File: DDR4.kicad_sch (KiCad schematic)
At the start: 37 parts, among them U14 2199155-1

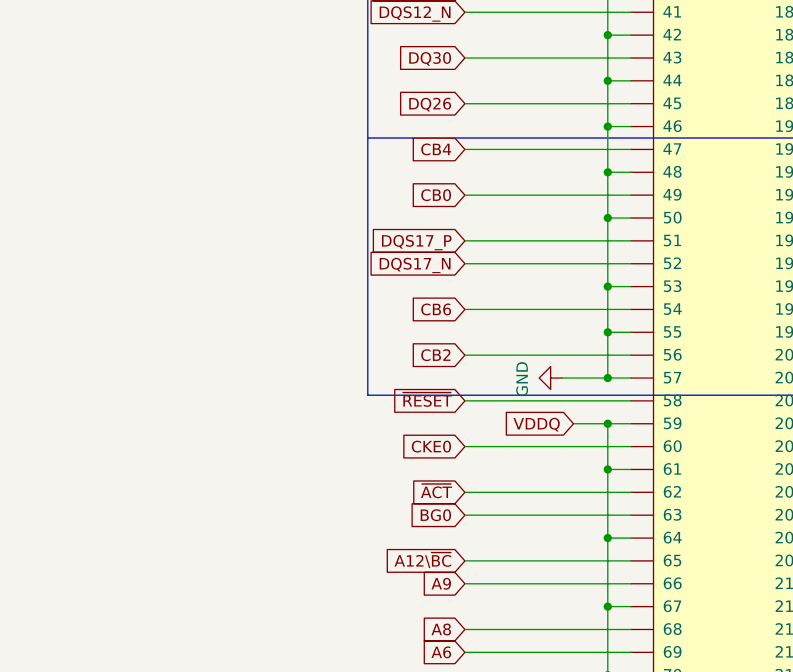
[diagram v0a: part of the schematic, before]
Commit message: Added hot-swap: button, LED indication, detection on ground pin. Updated SN74LVC1G07 symbol
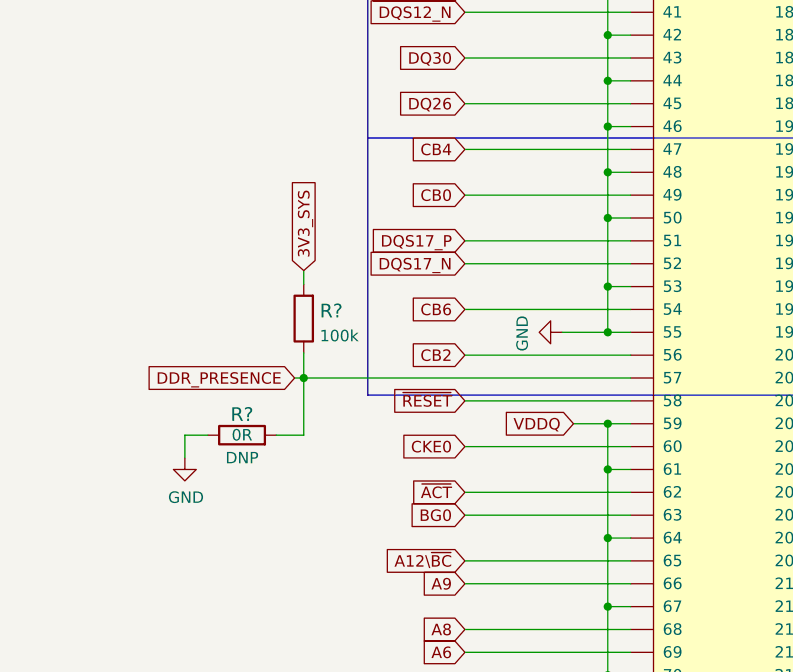
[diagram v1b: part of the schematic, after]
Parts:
- added R?: R_0R_0402, antmicro-footprints:0402-res, symbol antmicroResistors0402:R_0R_0402
- added R?: R_100k_0402, antmicro-footprints:0402-res, symbol antmicroResistors0402:R_100k_0402
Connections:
- net GND: now also R?.1; no longer U14.57
- new net 3V3_SYS: R?.2
- new net DDR_PRESENCE: R?.1, R?.2, U14.57
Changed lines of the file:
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@@
   (junction (at 125.73 168.91) (diameter 0) (color 0 0 0 0)
   )
-  (junction (at 97.79 194.31) (diameter 0) (color 0 0 0 0)
-  )
   (junction (at 97.79 189.23) (diameter 0) (color 0 0 0 0)
   )
@@
   (junction (at 125.73 179.07) (diameter 0) (color 0 0 0 0)
   )
+  (junction (at 64.008 194.31) (diameter 0) (color 0 0 0 0)
+  )
   (junction (at 259.715 175.895) (diameter 0) (color 0 0 0 0)
   )
@@
     (stroke (width 0) (type default) (color 0 0 0 0))
   )
-  (wire (pts (xy 97.79 194.31) (xy 92.71 194.31))
+  (wire (pts (xy 97.79 189.23) (xy 92.71 189.23))
     (stroke (width 0) (type default) (color 0 0 0 0))
   )
@@
     (stroke (width 0) (type default) (color 0 0 0 0))
   )
-  (wire (pts (xy 97.79 194.31) (xy 97.79 189.23))
-    (stroke (width 0) (type default) (color 0 0 0 0))
-  )
   (wire (pts (xy 259.715 86.995) (xy 259.715 81.915))
     (stroke (width 0) (type default) (color 0 0 0 0))
@@
     (stroke (width 0) (type default) (color 0 0 0 0))
   )
+  (wire (pts (xy 60.96 200.66) (xy 64.008 200.66))
+    (stroke (width 0) (type default) (color 0 0 0 0))
+  )
   (wire (pts (xy 287.655 137.795) (xy 285.115 137.795))
     (stroke (width 0) (type default) (color 0 0 0 0))
@@
     (stroke (width 0) (type default) (color 0 0 0 0))
   )
+  (wire (pts (xy 50.8 200.66) (xy 53.34 200.66))
+    (stroke (width 0) (type default) (color 0 0 0 0))
+  )
   (wire (pts (xy 285.115 219.075) (xy 303.53 219.075))
     (stroke (width 0) (type default) (color 0 0 0 0))
@@
     (stroke (width 0) (type default) (color 0 0 0 0))
   )
+  (wire (pts (xy 64.008 200.66) (xy 64.008 194.31))
+    (stroke (width 0) (type default) (color 0 0 0 0))
+  )
   (wire (pts (xy 123.19 242.57) (xy 128.27 242.57))
     (stroke (width 0) (type default) (color 0 0 0 0))
@@
     (stroke (width 0) (type default) (color 0 0 0 0))
   )
+  (wire (pts (xy 64.008 182.372) (xy 64.008 183.896))
+    (stroke (width 0) (type default) (color 0 0 0 0))
+  )
   (wire (pts (xy 287.655 155.575) (xy 287.655 160.655))
     (stroke (width 0) (type default) (color 0 0 0 0))
@@
     (stroke (width 0) (type default) (color 0 0 0 0))
   )
+  (wire (pts (xy 50.8 203.2) (xy 50.8 200.66))
+    (stroke (width 0) (type default) (color 0 0 0 0))
+  )
   (wire (pts (xy 97.79 128.27) (xy 97.79 120.65))
     (stroke (width 0) (type default) (color 0 0 0 0))
@@
     (stroke (width 0) (type default) (color 0 0 0 0))
   )
-  (wire (pts (xy 100.33 194.31) (xy 97.79 194.31))
+  (wire (pts (xy 64.008 194.31) (xy 100.33 194.31))
+    (stroke (width 0) (type default) (color 0 0 0 0))
+  )
+  (wire (pts (xy 62.992 194.31) (xy 64.008 194.31))
     (stroke (width 0) (type default) (color 0 0 0 0))
   )
@@
     (stroke (width 0) (type default) (color 0 0 0 0))
   )
+  (wire (pts (xy 64.008 194.31) (xy 64.008 191.516))
+    (stroke (width 0) (type default) (color 0 0 0 0))
+  )
   (wire (pts (xy 347.98 238.125) (xy 354.965 238.125))
     (stroke (width 0) (type default) (color 0 0 0 0))
@@
     )
   )
+  (global_label "3V3_SYS" (shape input) (at 64.008 182.372 90) (fields_autoplaced)
+    (effects (font (size 1.27 1.27)) (justify left))
+    (property "Intersheet References" "${INTERSHEET_REFS}" (id 0) (at -88.392 -29.083 0)
+      (effects (font (size 1.27 1.27)) hide)
+    )
+  )
   (global_label "DQ39" (shape input) (at 303.53 120.015 0) (fields_autoplaced)
     (effects (font (size 1.27 1.27)) (justify left))
@@
     )
   )
+  (global_label "DDR_PRESENCE" (shape input) (at 62.992 194.31 180) (fields_autoplaced)
+    (effects (font (size 1.27 1.27)) (justify right))
+    (property "Intersheet References" "${INTERSHEET_REFS}" (id 0) (at 46.093 194.2306 0)
+      (effects (font (size 1.27 1.27)) (justify right) hide)
+    )
+  )
   (global_label "~{SAVE}" (shape input) (at 303.53 76.835 0) (fields_autoplaced)
     (effects (font (size 1.27 1.27)) (justify left))
@@
     (pin "1")
   )
-  (symbol (lib_id "data-center-dram-tester:GND") (at 92.71 194.31 270) (unit 1)
+  (symbol (lib_id "data-center-dram-tester:GND") (at 92.71 189.23 270) (unit 1)
     (in_bom yes) (on_board yes)
-    (property "Reference" "#PWR0150" (id 0) (at 86.36 194.31 0)
+    (property "Reference" "#PWR0150" (id 0) (at 86.36 189.23 0)
       (effects (font (size 1.27 1.27)) hide)
     )
-    (property "Value" "GND" (id 1) (at 88.3158 194.437 0))
-    (property "Footprint" "" (id 2) (at 92.71 194.31 0)
+    (property "Value" "GND" (id 1) (at 88.3158 189.357 0))
+    (property "Footprint" "" (id 2) (at 92.71 189.23 0)
       (effects (font (size 1.27 1.27)) hide)
     )
-    (property "Datasheet" "" (id 3) (at 92.71 194.31 0)
+    (property "Datasheet" "" (id 3) (at 92.71 189.23 0)
       (effects (font (size 1.27 1.27)) hide)
     )
@@
     (pin "1")
     (pin "2")
+  )
+  (symbol (lib_id "antmicroResistors0402:R_0R_0402") (at 57.15 200.66 0) (unit 1)
+    (in_bom yes) (on_board yes)
+    (property "Reference" "R?" (id 0) (at 57.15 198.374 0)
+      (effects (font (size 1.524 1.524)))
+    )
+    (property "Value" "R_0R_0402" (id 1) (at 57.15 204.47 0)
+      (effects (font (size 1.524 1.524)) hide)
+    )
+    (property "Footprint" "antmicro-footprints:0402-res" (id 2) (at 62.23 195.58 0)
+      (effects (font (size 1.524 1.524)) (justify left) hide)
+    )
+    (property "Datasheet" "" (id 3) (at 57.15 200.66 0)
+      (effects (font (size 1.27 1.27)) hide)
+    )
+    (property "Manufacturer" "PANASONIC" (id 4) (at 62.23 190.5 0)
+      (effects (font (size 1.524 1.524)) (justify left) hide)
+    )
+    (property "MPN" "ERJ2GE0R00X" (id 5) (at 62.23 193.04 0)
+      (effects (font (size 1.524 1.524)) (justify left) hide)
+    )
+    (property "Val" "0R" (id 6) (at 57.15 200.66 0))
+    (property "DNP" "DNP" (id 7) (at 57.15 203.2 0))
+    (pin "1")
+    (pin "2")
+  )
+  (symbol (lib_id "data-center-dram-tester:GND") (at 50.8 203.2 0) (unit 1)
+    (in_bom yes) (on_board yes)
+    (property "Reference" "#PWR?" (id 0) (at 50.8 209.55 0)
+      (effects (font (size 1.27 1.27)) hide)
+    )
+    (property "Value" "GND" (id 1) (at 50.927 207.5942 0))
+    (property "Footprint" "" (id 2) (at 50.8 203.2 0)
+      (effects (font (size 1.27 1.27)) hide)
+    )
+    (property "Datasheet" "" (id 3) (at 50.8 203.2 0)
+      (effects (font (size 1.27 1.27)) hide)
+    )
+    (pin "1")
+  )
+  (symbol (lib_id "antmicroResistors0402:R_100k_0402") (at 64.008 187.706 90) (unit 1)
+    (in_bom yes) (on_board yes) (fields_autoplaced)
+    (property "Reference" "R?" (id 0) (at 65.786 186.8714 90)
+      (effects (font (size 1.524 1.524)) (justify right))
+    )
+    (property "Value" "R_100k_0402" (id 1) (at 67.818 187.706 0)
+      (effects (font (size 1.524 1.524)) hide)
+    )
+    (property "Footprint" "antmicro-footprints:0402-res" (id 2) (at 58.928 182.626 0)
+      (effects (font (size 1.524 1.524)) (justify left) hide)
+    )
+    (property "Datasheet" "" (id 3) (at 64.008 187.706 0)
+      (effects (font (size 1.27 1.27)) hide)
+    )
+    (property "Manufacturer" "VISHAY" (id 4) (at 53.848 182.626 0)
+      (effects (font (size 1.524 1.524)) (justify left) hide)
+    )
+    (property "MPN" "CRCW0402100KFKEDHP" (id 5) (at 56.388 182.626 0)
+      (effects (font (size 1.524 1.524)) (justify left) hide)
+    )
+    (property "Val" "100k" (id 6) (at 65.786 189.6365 90)
+      (effects (font (size 1.27 1.27)) (justify right))
+    )
+    (pin "1")
+    (pin "2")

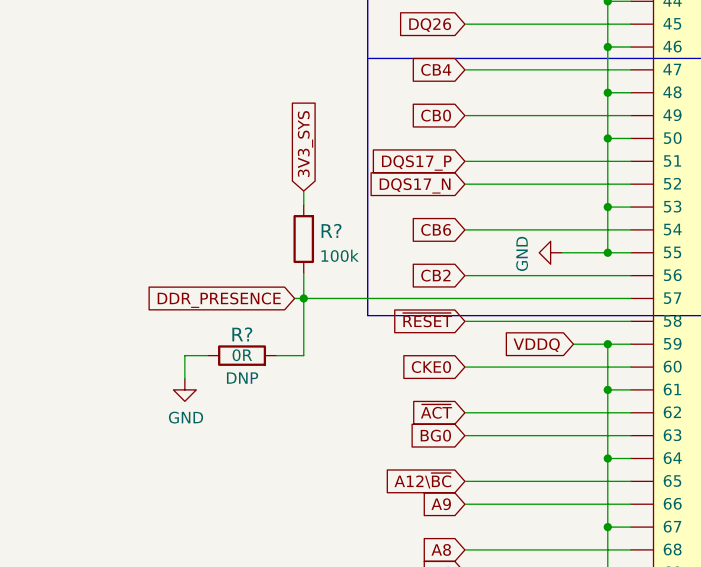
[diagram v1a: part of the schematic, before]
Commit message: Connect ETH mux, connect AUX_JTAG to FMC connector, add RC filter for HOT_SWAP_BUTTON signal
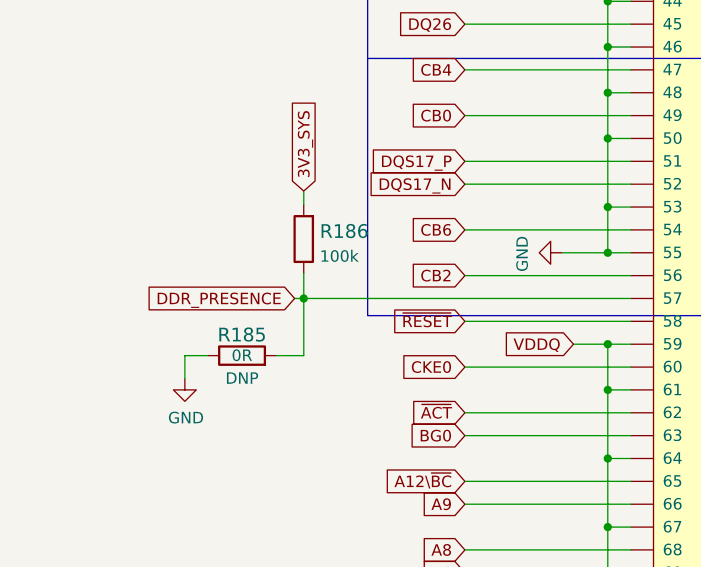
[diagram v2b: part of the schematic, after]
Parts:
- gave numbers to parts that had none: 2
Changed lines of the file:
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@@
   (symbol (lib_id "antmicroResistors0402:R_0R_0402") (at 57.15 200.66 0) (unit 1)
     (in_bom yes) (on_board yes)
-    (property "Reference" "R?" (id 0) (at 57.15 198.374 0)
+    (property "Reference" "R185" (id 0) (at 57.15 198.374 0)
       (effects (font (size 1.524 1.524)))
     )
@@
   (symbol (lib_id "data-center-dram-tester:GND") (at 50.8 203.2 0) (unit 1)
     (in_bom yes) (on_board yes)
-    (property "Reference" "#PWR?" (id 0) (at 50.8 209.55 0)
+    (property "Reference" "#PWR0317" (id 0) (at 50.8 209.55 0)
       (effects (font (size 1.27 1.27)) hide)
     )
@@
   (symbol (lib_id "antmicroResistors0402:R_100k_0402") (at 64.008 187.706 90) (unit 1)
     (in_bom yes) (on_board yes) (fields_autoplaced)
-    (property "Reference" "R?" (id 0) (at 65.786 186.8714 90)
+    (property "Reference" "R186" (id 0) (at 65.786 186.8714 90)
       (effects (font (size 1.524 1.524)) (justify right))
     )

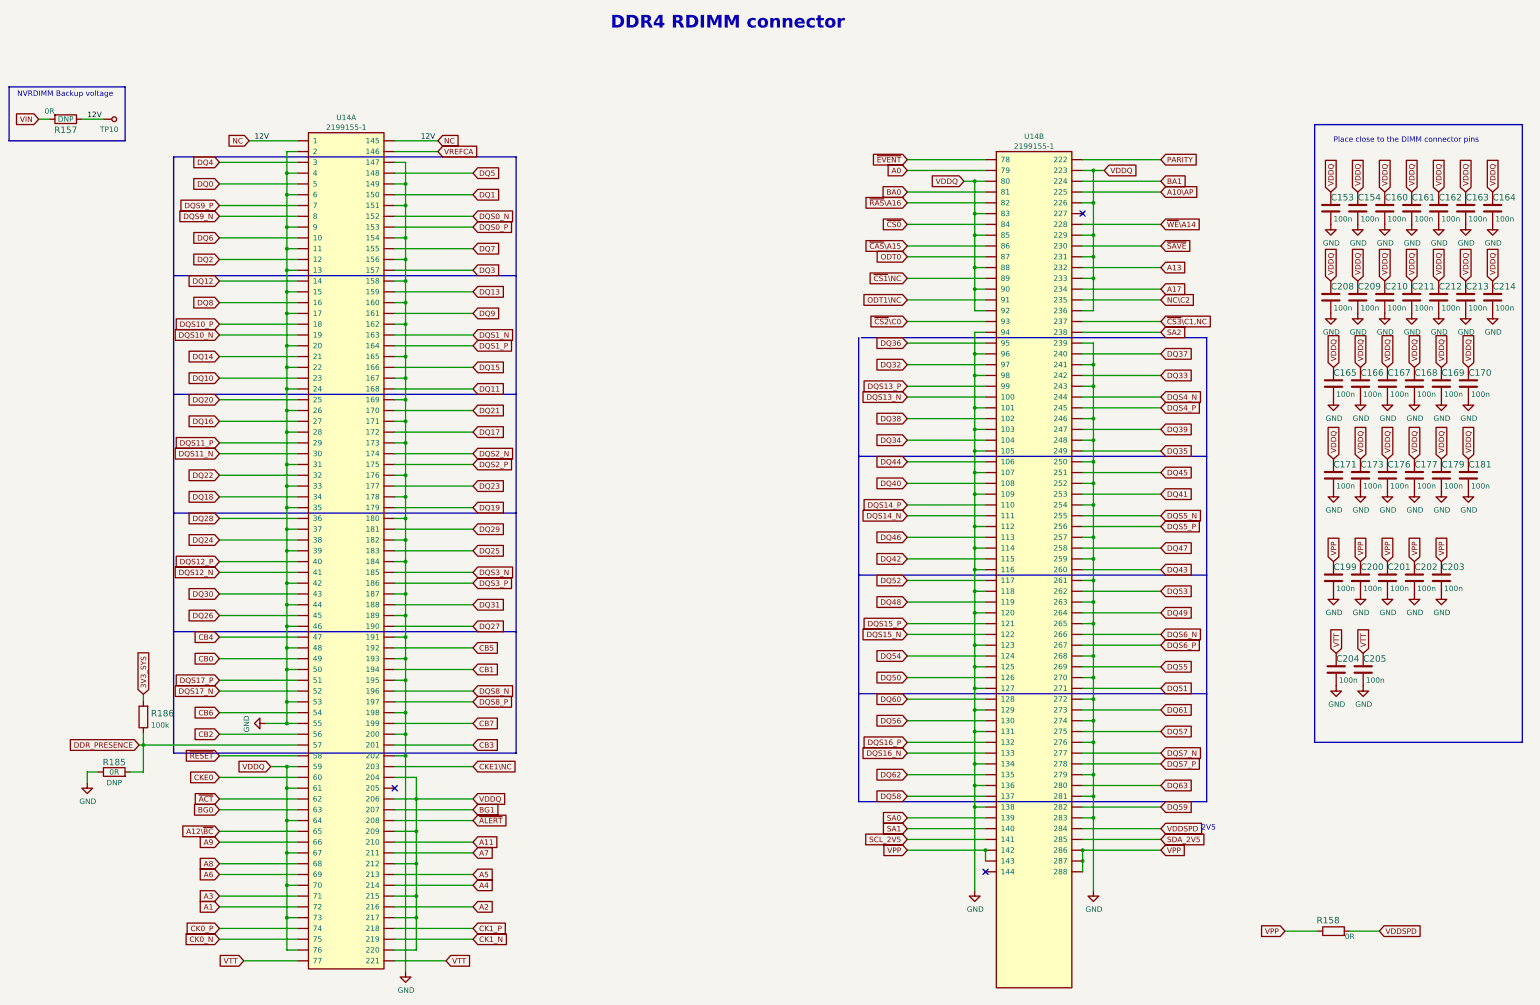
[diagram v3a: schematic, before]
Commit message: Readability improvements
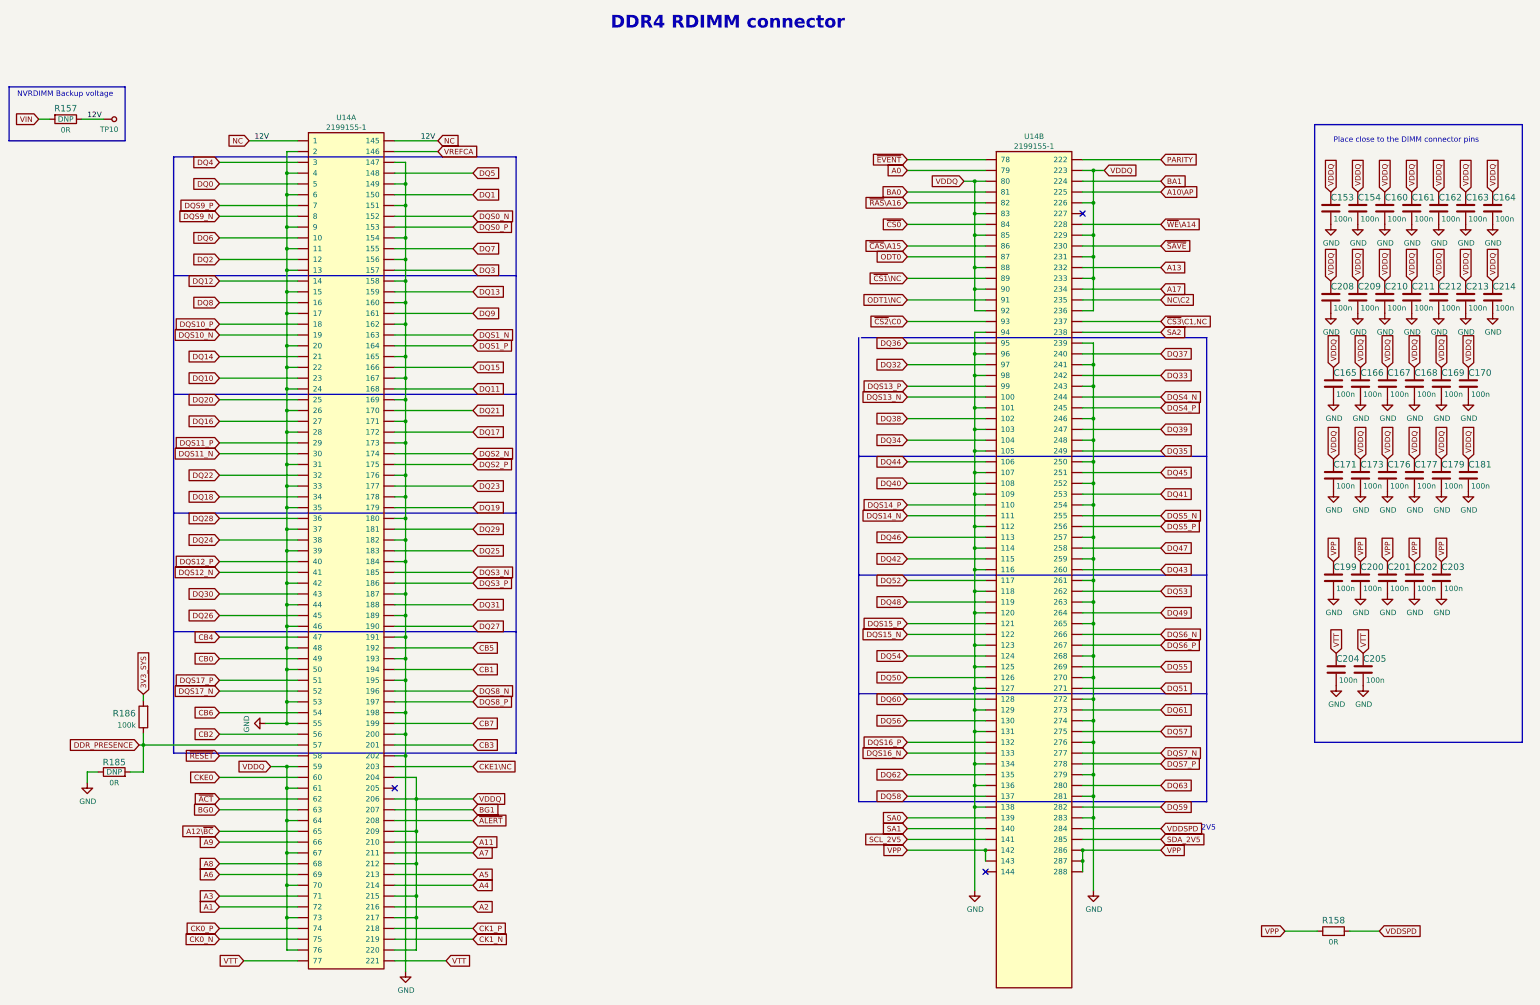
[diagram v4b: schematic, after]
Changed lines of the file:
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@@
   (symbol (lib_id "data-center-dram-tester:R_0R_0603") (at 45.72 46.99 180) (unit 1)
     (in_bom yes) (on_board yes)
-    (property "Reference" "R157" (id 0) (at 45.72 49.53 0)
+    (property "Reference" "R157" (id 0) (at 45.72 44.45 0)
       (effects (font (size 1.524 1.524)))
     )
@@
       (effects (font (size 1.524 1.524)) (justify left) hide)
     )
-    (property "Val" "0R" (id 6) (at 41.91 45.085 0))
+    (property "Val" "0R" (id 6) (at 45.72 49.53 0))
     (property "DNP" "DNP" (id 7) (at 45.72 46.99 0))
     (pin "1")
@@
   (symbol (lib_id "data-center-dram-tester:R_0R_0603") (at 344.17 238.125 0) (unit 1)
     (in_bom yes) (on_board yes)
-    (property "Reference" "R158" (id 0) (at 342.9 235.585 0)
+    (property "Reference" "R158" (id 0) (at 344.17 235.585 0)
       (effects (font (size 1.524 1.524)))
     )
@@
       (effects (font (size 1.524 1.524)) (justify left) hide)
     )
-    (property "Val" "0R" (id 6) (at 347.98 239.395 0))
+    (property "Val" "0R" (id 6) (at 344.17 240.665 0))
     (pin "1")
     (pin "2")
@@
       (effects (font (size 1.524 1.524)) (justify left) hide)
     )
-    (property "Val" "0R" (id 6) (at 57.15 200.66 0))
-    (property "DNP" "DNP" (id 7) (at 57.15 203.2 0))
+    (property "Val" "0R" (id 6) (at 57.15 203.2 0))
+    (property "DNP" "DNP" (id 7) (at 57.15 200.66 0))
     (pin "1")
     (pin "2")
@@
   (symbol (lib_id "antmicroResistors0402:R_100k_0402") (at 64.008 187.706 90) (unit 1)
     (in_bom yes) (on_board yes) (fields_autoplaced)
-    (property "Reference" "R186" (id 0) (at 65.786 186.8714 90)
-      (effects (font (size 1.524 1.524)) (justify right))
+    (property "Reference" "R186" (id 0) (at 62.23 186.8714 90)
+      (effects (font (size 1.524 1.524)) (justify left))
     )
     (property "Value" "R_100k_0402" (id 1) (at 67.818 187.706 0)
@@
       (effects (font (size 1.524 1.524)) (justify left) hide)
     )
-    (property "Val" "100k" (id 6) (at 65.786 189.6365 90)
-      (effects (font (size 1.27 1.27)) (justify right))
-    )
-    (pin "1")
+    (property "Val" "100k" (id 6) (at 62.23 189.6365 90)
+      (effects (font (size 1.27 1.27)) (justify left))
+    )
+    (pin "1")
